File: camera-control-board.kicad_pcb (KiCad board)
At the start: 4 copper layers, 96 x 90 mm, 51 parts, among them J1 DF12NB-36DS-0.5V_51_, J2 10104110-0001LF, J3 104031-0811, J4 02x05 M 1.27mm, J5 Conn_01x09, SW1 CAS-120TA, SW3 SW_Push, U1 STM32H743IITx, U2 IS42S32800J-7TLI, U3 W25Q256JVEIQ TR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

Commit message: Layout ~1/3rd done
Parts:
- moved U1 29.4 mm to (74.8, 143.2)
- moved U2 26.8 mm to (103.3, 143.2)
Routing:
- net /DRAM_D14: track 80.5 -> 1.08 mm, vias 2 -> 0
- net /DRAM_WE: track 0.00 -> 55.9 mm, vias 0 -> 2
- net /DRAM_D0: track 0.00 -> 55.1 mm
- net /DRAM_D1: track 0.00 -> 54.6 mm
- net /DRAM_D4: track 0.00 -> 53.0 mm, vias 0 -> 2
- net /DRAM_D5: track 0.00 -> 53.0 mm, vias 0 -> 2
- net /DRAM_D7: track 0.00 -> 53.0 mm, vias 0 -> 2
- net /DRAM_D6: track 0.00 -> 53.0 mm, vias 0 -> 2
- net /DRAM_D2: track 0.00 -> 53.0 mm, vias 0 -> 2
- net /DRAM_RAS: track 0.00 -> 53.0 mm, vias 0 -> 2
- net /DRAM_D3: track 0.00 -> 52.9 mm, vias 0 -> 2
- net /DRAM_DQM0: track 0.00 -> 52.9 mm, vias 0 -> 2
- net /DRAM_BA1: track 0.00 -> 52.7 mm, vias 0 -> 2
- net /DRAM_BA0: track 0.00 -> 52.7 mm, vias 0 -> 2
- net /DRAM_CAS: track 0.00 -> 52.7 mm, vias 0 -> 2
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
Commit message: attempting layout on diff branch
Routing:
- net /DRAM_D21: track 0.00 -> 54.3 mm, vias 0 -> 2
- net /DRAM_D23: track 0.00 -> 41.3 mm, vias 0 -> 2
- net /DRAM_D22: track 0.00 -> 40.7 mm, vias 0 -> 2
- net /DRAM_D19: track 0.00 -> 38.6 mm, vias 0 -> 2
- net /DRAM_D18: track 32.2 -> 52.6 mm
- net /DRAM_D16: track 31.8 -> 50.0 mm
- net /DRAM_DQM2: track 43.6 -> 53.0 mm
- net /DRAM_A2: track 44.9 -> 53.0 mm
- net /DRAM_CS: track 45.6 -> 53.0 mm
- net /DRAM_A1: track 45.7 -> 52.9 mm
- net /DRAM_A0: track 46.7 -> 53.0 mm
- net /DRAM_D17: track 33.1 -> 39.1 mm
- net /DRAM_A11: track 47.7 -> 53.0 mm
- net /DRAM_D20: track 0.00 -> 5.04 mm, vias 0 -> 2
- net /DRAM_WE: track 55.9 -> 53.1 mm
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
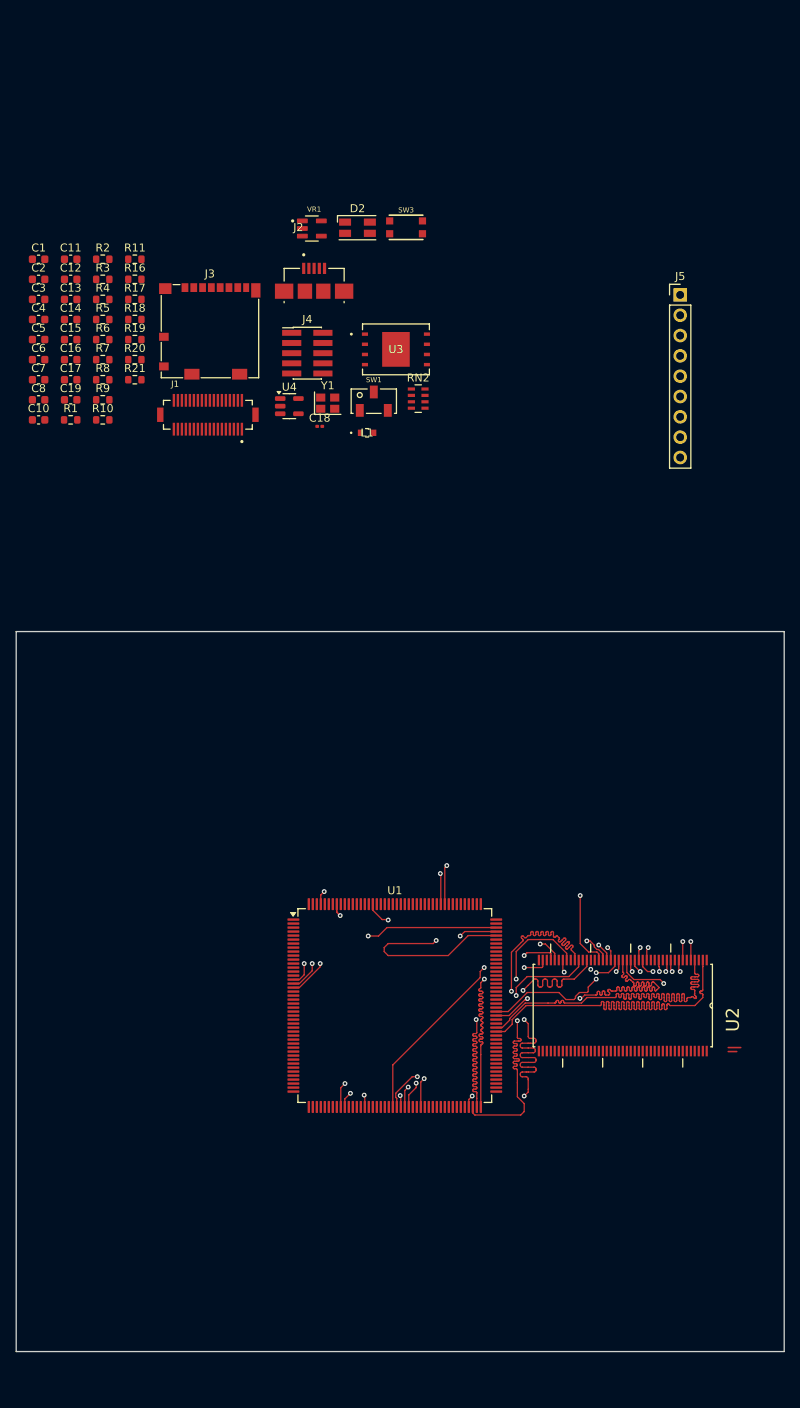
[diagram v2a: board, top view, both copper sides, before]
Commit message: layout 45deg
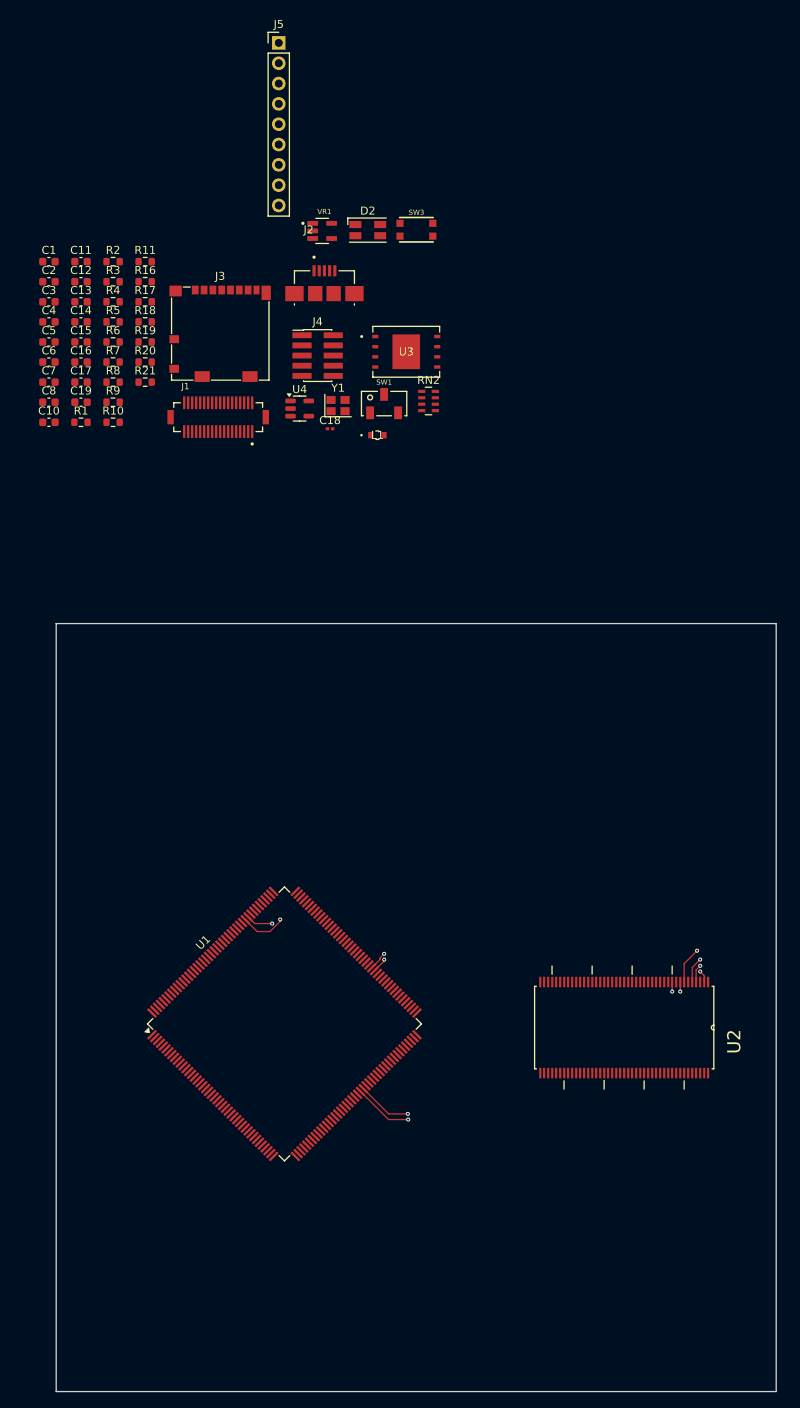
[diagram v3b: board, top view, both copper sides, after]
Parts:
- moved J5 59.2 mm to (60.3, 22.9)
- moved U1 14.0 mm to (61.0, 145.5), turned to 45 degrees
- moved U2 2.76 mm to (103.5, 146.0)
- moved C18 1.32 mm to (66.7, 71.2)
- moved L1 1.32 mm to (72.7, 72.0)
- moved RN2 1.32 mm to (79.0, 67.7)
- moved J2 1.32 mm to (66.0, 54.3)
- moved VR1 1.32 mm to (65.7, 46.4)
- moved D2 1.32 mm to (71.5, 46.3)
- moved J4 1.32 mm to (65.2, 62.0)
- moved SW3 1.32 mm to (77.5, 46.3)
- moved Y1 1.32 mm to (67.7, 68.2)
- moved C12 1.32 mm to (35.6, 52.8)
- moved C13 1.32 mm to (35.6, 55.3)
- moved C16 1.32 mm to (35.6, 62.8)
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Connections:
- net /DRAM_CLK renamed /DRAM_CLOCK
- U1 pad 12: unconnected-(U1-PI10-Pad12) -> /DRAM_D31
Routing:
- net /DRAM_D21: track 54.3 -> 0.00 mm, vias 2 -> 0
- net /DRAM_WE: track 53.1 -> 0.00 mm, vias 2 -> 0
- net /DRAM_D7: track 53.0 -> 0.00 mm, vias 2 -> 0
- net /DRAM_A11: track 53.0 -> 0.00 mm, vias 2 -> 0
- net /DRAM_A0: track 53.0 -> 0.00 mm, vias 2 -> 0
- net /DRAM_D6: track 53.0 -> 0.00 mm, vias 2 -> 0
- net /DRAM_DQM2: track 53.0 -> 0.00 mm, vias 2 -> 0
- net /DRAM_RAS: track 53.0 -> 0.00 mm, vias 2 -> 0
- net /DRAM_A2: track 53.0 -> 0.00 mm, vias 2 -> 0
- net /DRAM_CS: track 53.0 -> 0.00 mm, vias 2 -> 0
- net /DRAM_DQM0: track 52.9 -> 0.00 mm, vias 2 -> 0
- net /DRAM_A1: track 52.9 -> 0.00 mm, vias 2 -> 0
- net /DRAM_BA0: track 52.7 -> 0.00 mm, vias 2 -> 0
- net /DRAM_CAS: track 52.7 -> 0.00 mm, vias 2 -> 0
- net /DRAM_BA1: track 52.6 -> 0.00 mm, vias 2 -> 0
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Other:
- board size 96 x 90 mm -> 90 x 96 mm

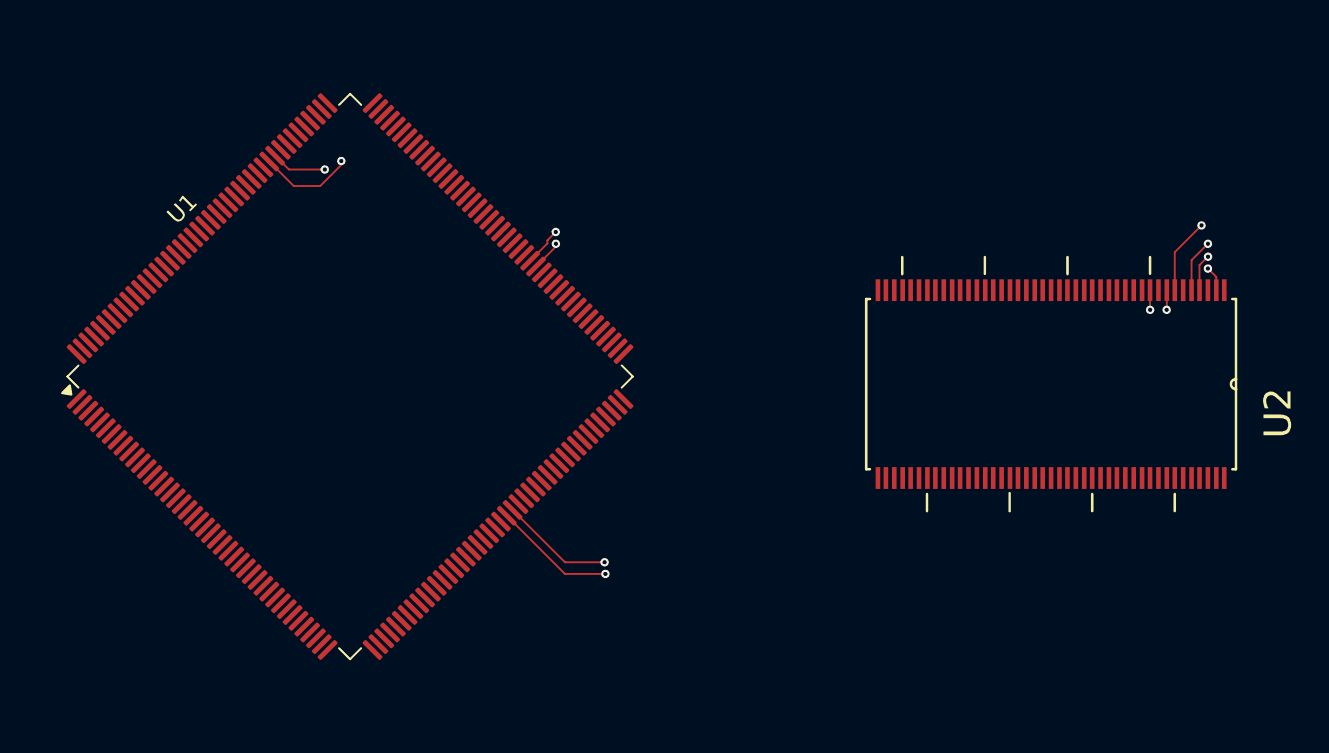
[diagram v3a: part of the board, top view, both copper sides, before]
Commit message: added 3v3, GND routing
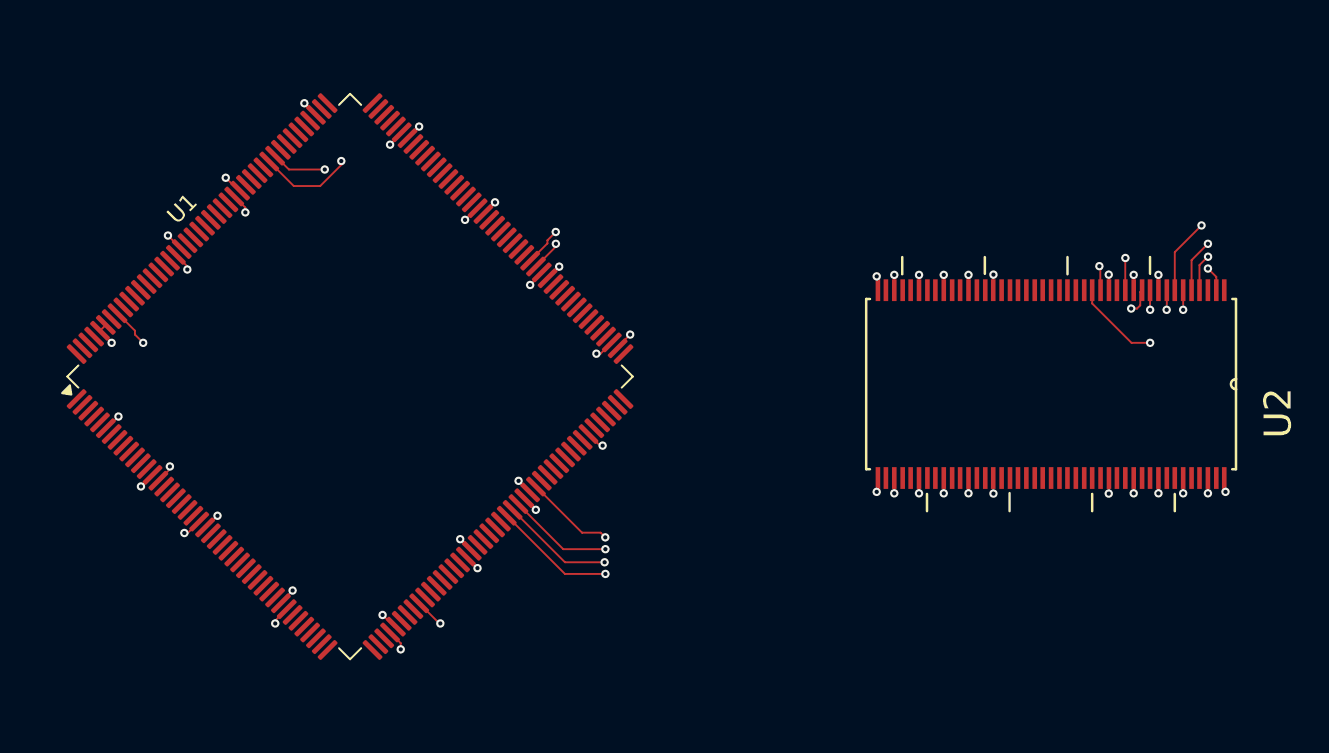
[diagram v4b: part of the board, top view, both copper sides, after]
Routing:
- net +3.3V: track 0.00 -> 175.7 mm, vias 0 -> 25
- net /DRAM_DQM0: track 0.00 -> 63.8 mm, vias 0 -> 2
- net /DRAM_WE: track 0.00 -> 57.1 mm, vias 0 -> 2
- net /DRAM_D7: track 0.00 -> 47.5 mm, vias 0 -> 2
- net /DRAM_D6: track 0.00 -> 45.9 mm, vias 0 -> 2
- net GND: track 0.00 -> 25.5 mm, vias 0 -> 25

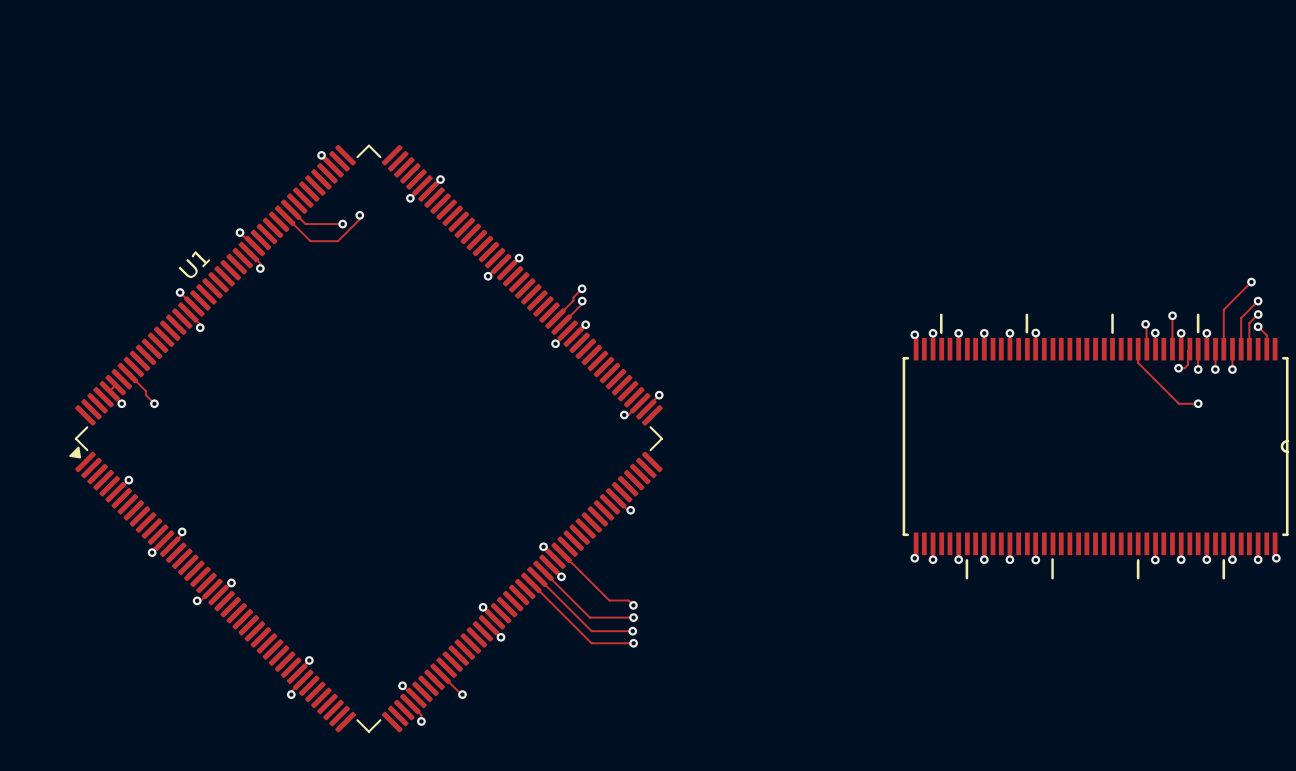
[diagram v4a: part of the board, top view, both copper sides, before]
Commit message: First half routed, impedance matching now
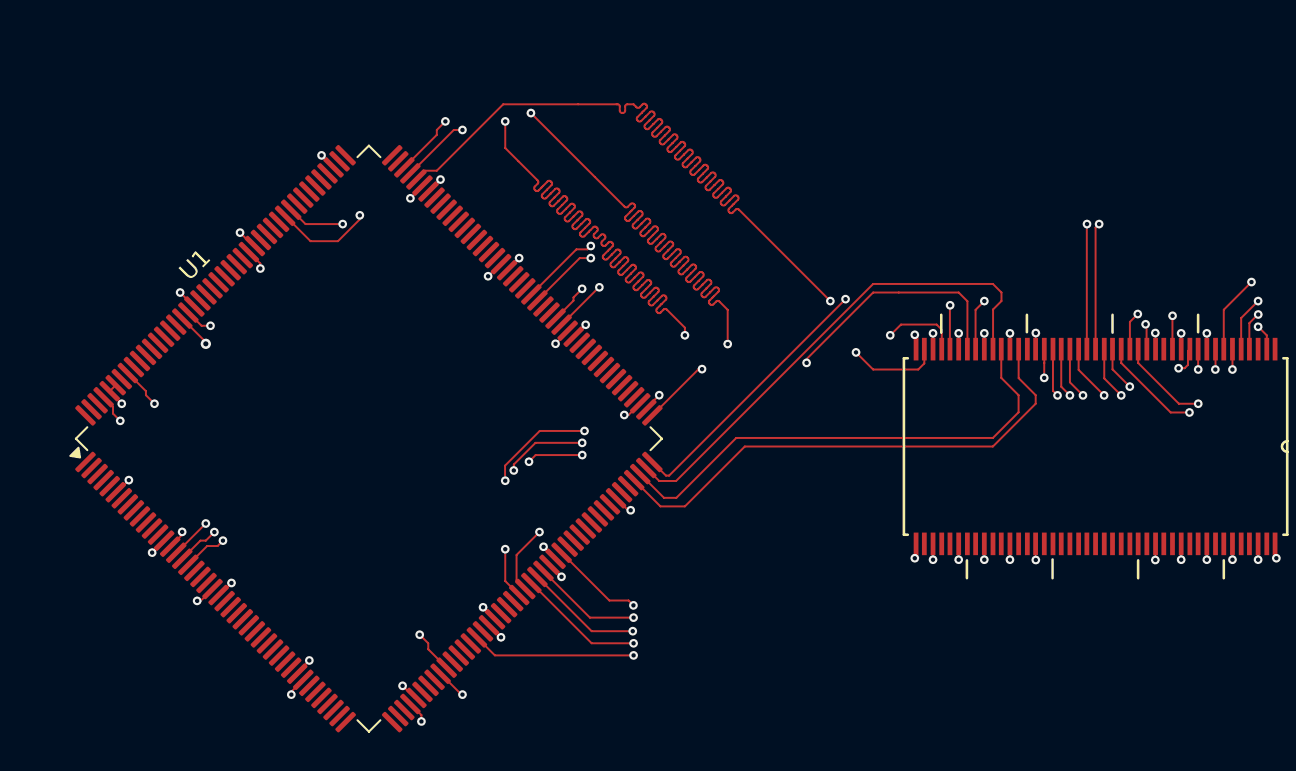
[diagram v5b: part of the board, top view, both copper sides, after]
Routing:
- net /DRAM_D22: track 0.00 -> 67.3 mm, vias 0 -> 4
- net /DRAM_D21: track 0.00 -> 64.2 mm, vias 0 -> 2
- net /DRAM_D23: track 0.00 -> 61.4 mm, vias 0 -> 4
- net /DRAM_A0: track 0.00 -> 59.8 mm, vias 0 -> 4
- net /DRAM_CAS: track 0.00 -> 59.5 mm, vias 0 -> 2
- net /DRAM_A1: track 0.00 -> 58.9 mm, vias 0 -> 4
- net /DRAM_DQM2: track 0.00 -> 58.5 mm, vias 0 -> 2
- net /DRAM_A2: track 0.00 -> 58.2 mm, vias 0 -> 4
- net /DRAM_CS: track 0.00 -> 54.5 mm, vias 0 -> 2
- net /DRAM_RAS: track 0.00 -> 54.0 mm, vias 0 -> 2
- net /DRAM_A10: track 0.00 -> 47.5 mm, vias 0 -> 2
- net /DRAM_A11: track 0.00 -> 47.5 mm, vias 0 -> 2
- net /DRAM_BA0: track 0.00 -> 42.1 mm, vias 0 -> 2
- net /DRAM_BA1: track 0.00 -> 41.5 mm, vias 0 -> 2
- net /DRAM_D16: track 0.00 -> 30.2 mm
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
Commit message: AAAAAAAAAAAAAAAAAH
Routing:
- net /DRAM_DQM1: track 0.00 -> 64.9 mm, vias 0 -> 2
- net /DRAM_DQM3: track 0.00 -> 62.1 mm, vias 0 -> 2
- net /DRAM_D29: track 0.00 -> 62.0 mm, vias 0 -> 4
- net /DRAM_D28: track 0.00 -> 60.2 mm, vias 0 -> 4
- net /DRAM_A7: track 0.00 -> 58.4 mm, vias 0 -> 6
- net /DRAM_CLOCK: track 0.00 -> 58.2 mm, vias 0 -> 4
- net /DRAM_D13: track 0.00 -> 55.5 mm, vias 0 -> 2
- net /DRAM_D15: track 0.00 -> 55.5 mm, vias 0 -> 2
- net /DRAM_D12: track 0.00 -> 54.3 mm, vias 0 -> 4
- net /DRAM_D9: track 0.00 -> 53.4 mm, vias 0 -> 4
- net /DRAM_D8: track 0.00 -> 52.8 mm, vias 0 -> 2
- net /DRAM_D14: track 0.00 -> 51.8 mm, vias 0 -> 2
- net /DRAM_D11: track 0.00 -> 47.5 mm, vias 0 -> 4
- net /DRAM_D10: track 0.00 -> 47.3 mm, vias 0 -> 4
- net /DRAM_A8: track 0.00 -> 45.0 mm, vias 0 -> 4
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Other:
- copper layers 4 -> 6

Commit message: all first half impedance matched...,.
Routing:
- net /DRAM_D23: track 61.4 -> 64.2 mm
- net /DRAM_D22: track 61.4 -> 64.2 mm
- net /DRAM_D3: track 64.5 -> 65.9 mm
- net /DRAM_D2: track 64.5 -> 65.9 mm
- net /DRAM_D19: track 64.0 -> 65.4 mm
- net /DRAM_D4: track 64.3 -> 65.7 mm
- net /DRAM_BA1: track 64.2 -> 65.6 mm
- net /DRAM_WE: track 64.4 -> 65.8 mm
- net /DRAM_D21: track 64.2 -> 65.6 mm
- net /DRAM_CAS: track 64.4 -> 65.8 mm
- net /DRAM_A10: track 63.9 -> 65.3 mm
- net /DRAM_D0: track 64.2 -> 65.6 mm
- net /DRAM_DQM2: track 64.3 -> 65.7 mm
- net /DRAM_DQM0: track 64.5 -> 65.9 mm
- net /DRAM_CS: track 64.2 -> 65.6 mm
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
